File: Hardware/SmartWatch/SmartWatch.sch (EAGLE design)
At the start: 90 parts, among them T1 TESTPOINT-0603, T2 TESTPOINT-0603, T3 TESTPOINT-0603, T4 TESTPOINT-0603, T5 TESTPOINT-0603, U1 STM32L476, U10 MICRO-USB, U11 BNO055, U3 UG-2828GDEDF11, U4 FAN5331SX, U5 APDS-9960, U6 MCP73831, U7 AP2112K-3.3TRG-1, U8 ASDK-32.768, U9 ASCO-8

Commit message: updated PCB to 1.1 and added battery monitoring chip
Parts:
- removed R21: 10k, resistor:R-US_R0603
- added U12: MAX17048, SparkFun-DigitalIC:MAX17048DFN8
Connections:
- removed net PA14: U1PORTA.P15
- removed net STAT: R21.1, U1PORTA.P9, U6.STAT
- new net !ALRT: U12.!ALRT, U1PORTA.P15
- new net PA9: U1PORTA.P9
- net +3V3: no longer R21.2
- net GND: now also U12.CTG, U12.GND, U12.QSTRT
- net SCL: now also U12.SCL
- net SDA: now also U12.SDA
- net VBAT: now also U12.CELL, U12.VDD
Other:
- note added: "I2C ADDRESS = 0x36"
- moved on the sheet: BTN_BACK, BTN_BOOT0, BTN_DN, BTN_NRST, BTN_SEL, BTN_UP, C1, C10, C11, C12, C13, C14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

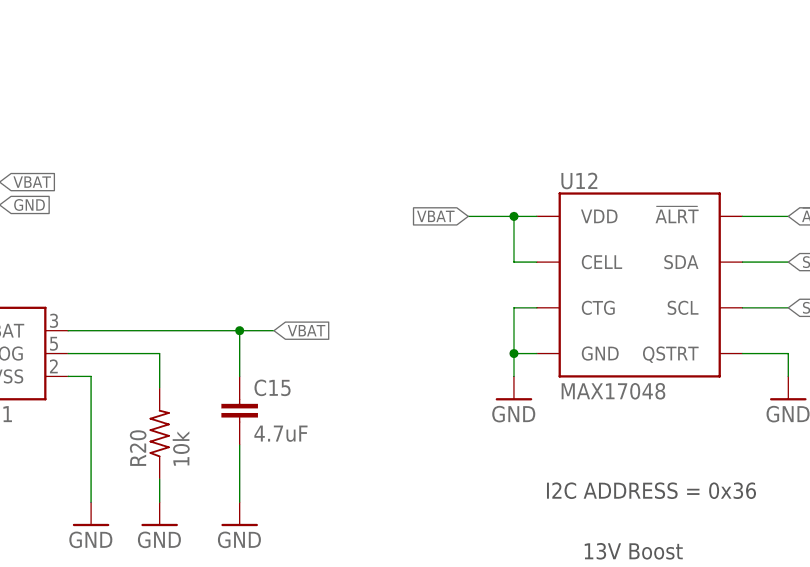
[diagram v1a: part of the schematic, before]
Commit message: added decoupling capacitor
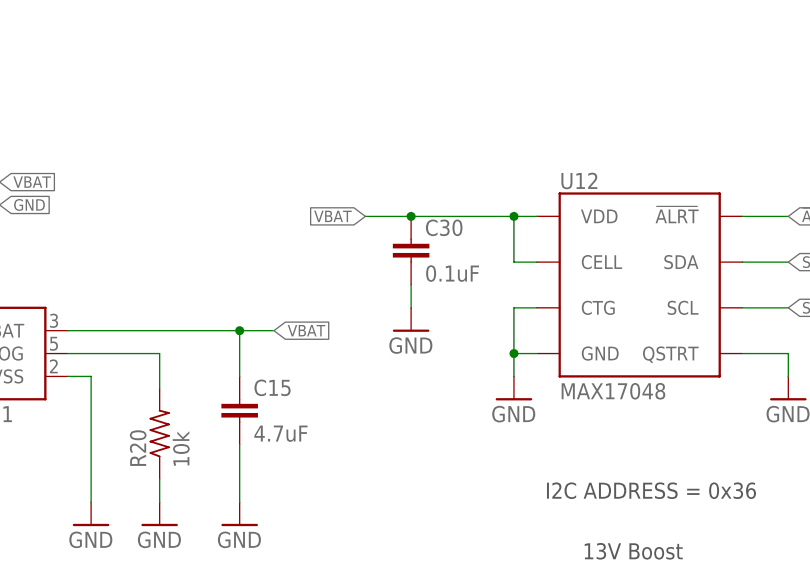
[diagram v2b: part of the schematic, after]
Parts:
- added C30: 0.1uF, resistor:C-EUC0603
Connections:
- net GND: now also C30.2
- net VBAT: now also C30.1
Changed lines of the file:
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@@
 <part name="GND19" library="SparkFun-Aesthetics" deviceset="GND" device=""/>
 <part name="GND21" library="SparkFun-Aesthetics" deviceset="GND" device=""/>
+<part name="C30" library="resistor" deviceset="C-EU" device="C0603" value="0.1uF">
+<attribute name="PROD_ID" value="CAP-08280"/>
+</part>
+<part name="GND22" library="SparkFun" deviceset="GND" device=""/>
 </parts>
 <sheets>
@@
 <instance part="GND19" gate="1" x="248.92" y="-21.59"/>
 <instance part="GND21" gate="1" x="218.44" y="-21.59"/>
+<instance part="C30" gate="G$1" x="207.01" y="-3.81">
+<attribute name="PROD_ID" x="207.01" y="-3.81" size="1.778" layer="96" display="off"/>
+</instance>
+<instance part="GND22" gate="1" x="207.01" y="-13.97"/>
 </instances>
 <busses>
@@
 <junction x="218.44" y="-16.51"/>
 </segment>
+<segment>
+<pinref part="C30" gate="G$1" pin="2"/>
+<pinref part="GND22" gate="1" pin="GND"/>
+<wire x1="207.01" y1="-11.43" x2="207.01" y2="-8.89" width="0.1524" layer="91"/>
+</segment>
 </net>
 <net name="BT_SCK" class="0">
@@
 <pinref part="U12" gate="G$1" pin="CELL"/>
 <wire x1="218.44" y1="-6.35" x2="220.98" y2="-6.35" width="0.1524" layer="91"/>
-<wire x1="218.44" y1="-1.27" x2="213.36" y2="-1.27" width="0.1524" layer="91"/>
+<wire x1="218.44" y1="-1.27" x2="207.01" y2="-1.27" width="0.1524" layer="91"/>
 <junction x="218.44" y="-1.27"/>
-<label x="213.36" y="-1.27" size="1.27" layer="95" rot="R180" xref="yes"/>
-</segment>
-</net>
+<label x="201.93" y="-1.27" size="1.27" layer="95" rot="R180" xref="yes"/>
+<pinref part="C30" gate="G$1" pin="1"/>
+<wire x1="207.01" y1="-1.27" x2="201.93" y2="-1.27" width="0.1524" layer="91"/>
+<junction x="207.01" y="-1.27"/>
+</segment>
+</net>

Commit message: updated bom
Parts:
- R23, R24, R25: value 10k -> 82
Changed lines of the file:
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@@
 <part name="D6" library="SparkFun-LED" deviceset="LED" device="0603"/>
 <part name="GND16" library="SparkFun" deviceset="GND" device=""/>
-<part name="R23" library="resistor" deviceset="R-US_" device="R0603" value="10k"/>
-<part name="R24" library="resistor" deviceset="R-US_" device="R0603" value="10k"/>
-<part name="R25" library="resistor" deviceset="R-US_" device="R0603" value="10k"/>
+<part name="R23" library="resistor" deviceset="R-US_" device="R0603" value="82"/>
+<part name="R24" library="resistor" deviceset="R-US_" device="R0603" value="82"/>
+<part name="R25" library="resistor" deviceset="R-US_" device="R0603" value="82"/>
 <part name="U12" library="SparkFun-DigitalIC" deviceset="MAX17048" device="DFN8" value="MAX17048">
 <attribute name="PROD_ID" value="IC-12551"/>
